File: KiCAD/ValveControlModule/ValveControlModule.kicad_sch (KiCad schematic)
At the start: 0 parts

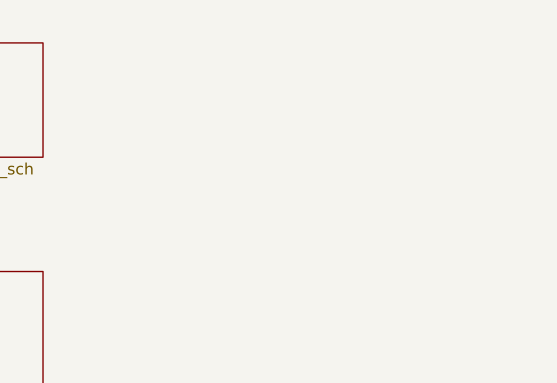
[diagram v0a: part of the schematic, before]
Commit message: 取り付け穴位置を更新
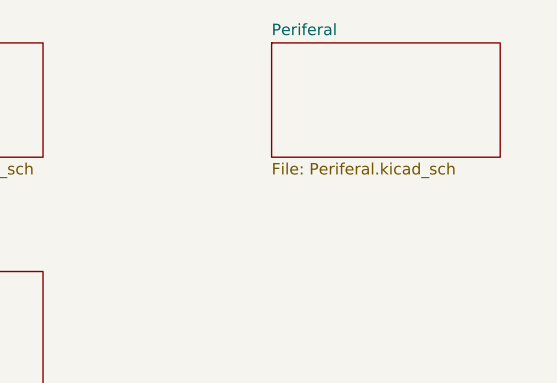
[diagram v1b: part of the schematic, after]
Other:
- added sheet Periferal (Periferal.kicad_sch)
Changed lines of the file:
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@@
+	)
+	(sheet
+		(at 127 38.1)
+		(size 25.4 12.7)
+		(exclude_from_sim no)
+		(in_bom yes)
+		(on_board yes)
+		(dnp no)
+		(fields_autoplaced yes)
+		(stroke
+			(width 0.1524)
+			(type solid)
+		)
+		(fill
+			(color 0 0 0 0.0000)
+		)
+		(property "Sheetname" "Periferal"
+			(at 127 37.3884 0)
+			(effects
+				(font
+					(size 1.27 1.27)
+				)
+				(justify left bottom)
+			)
+		)
+		(property "Sheetfile" "Periferal.kicad_sch"
+			(at 127 51.3846 0)
+			(effects
+				(font
+					(size 1.27 1.27)
+				)
+				(justify left top)
+			)
+		)
+		(instances
+			(project "ValveControlModule"
+				(path "/cd791ee8-0dde-470b-85a8-76474a846dd3"
+					(page "6")
+				)
+			)
+		)
 	)
 	(sheet
